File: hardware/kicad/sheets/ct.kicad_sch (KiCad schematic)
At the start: 30 parts, among them J12 CT, J13 AC_SENSE_DNP, U7 ADE7953ACPZ, Y1 3.579545MHz XO

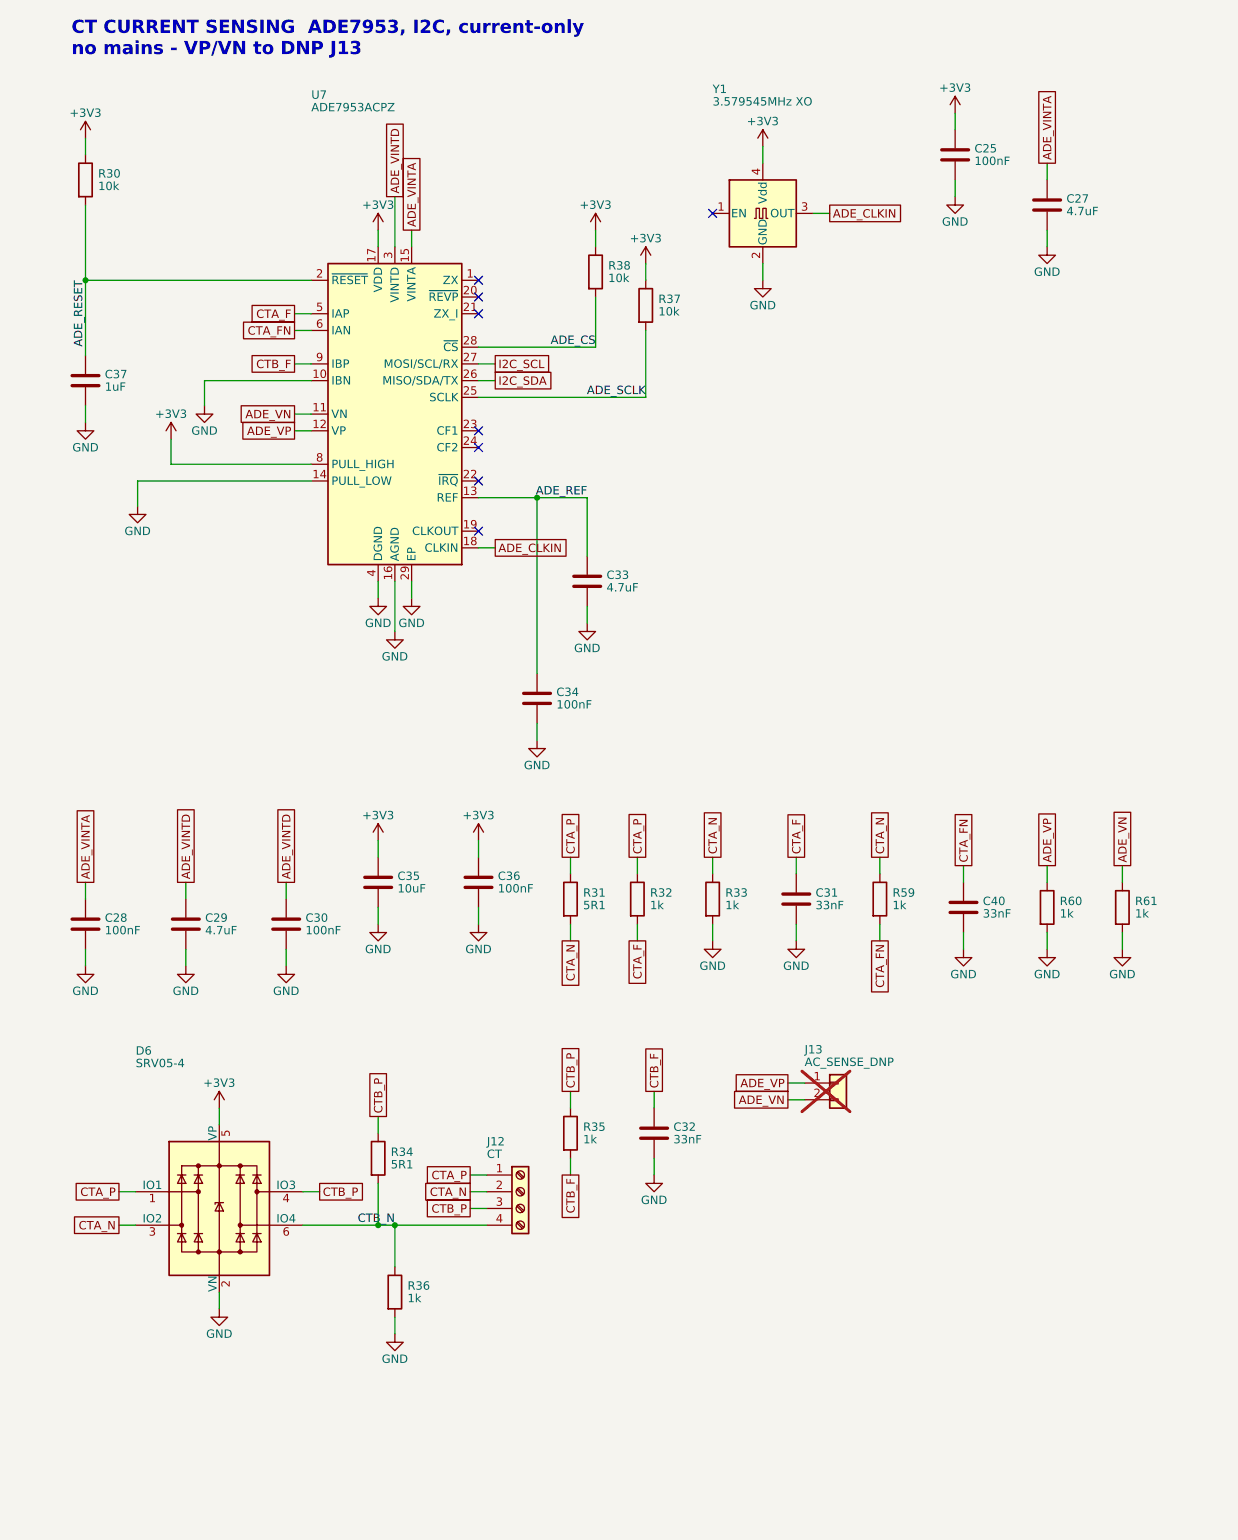
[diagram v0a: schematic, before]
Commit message: hardware: hierarchical schematic, ERC at 0/0, rev B.3
Applies items 1-3 of SCHEMATIC-REVIEW-2026-10-22.md.

ERC: the 173 lib_symbol_mismatch warnings were over-escaped quotes in the
embedded power symbols' Description strings; refreshed from the library.
The 18 off-grid power symbols are snapped and their stub wires redrawn.
The VIN and VLED global labels that existed only to carry a PWR_FLAG are
gone; the flags now sit on the nets they drive (J2.1, the VLED junction).
ERC reads 0 errors / 0 warnings with the documented SDO exclusion.

Hierarchy: no global labels remain. Each net that crosses sheets has one
hierarchical label per sheet, matching sheet pins on the root, and the
root wires those pins as a block diagram. Every other former global label
is a local label. The eight signal test points (TP4-TP11) move from the
test sheet to the mcu and ct sheets beside their nets, so the test block
needs no pins. KiCad names the nets /mcu/SPI_MISO etc.; netlist.py strips
the path, so the board's net names and the routing tables are unchanged
(182 components, 538 pads, 0 mismatches). single_global_label is now a
warning. check_sync_idempotent's collision fixture used the bare
"SPI_MISO" name and is updated, with a loud failure if its victims vanish.

Drawing: rev B.3 dated 2026-10-22 on every sheet, ct on A3 like the rest,
the three overflowing titles shortened, and the notes no longer refer to
design.py or to crystal load caps that no longer exist.

Co-Authored-By: Claude Fable 5.1 <noreply@anthropic.com>
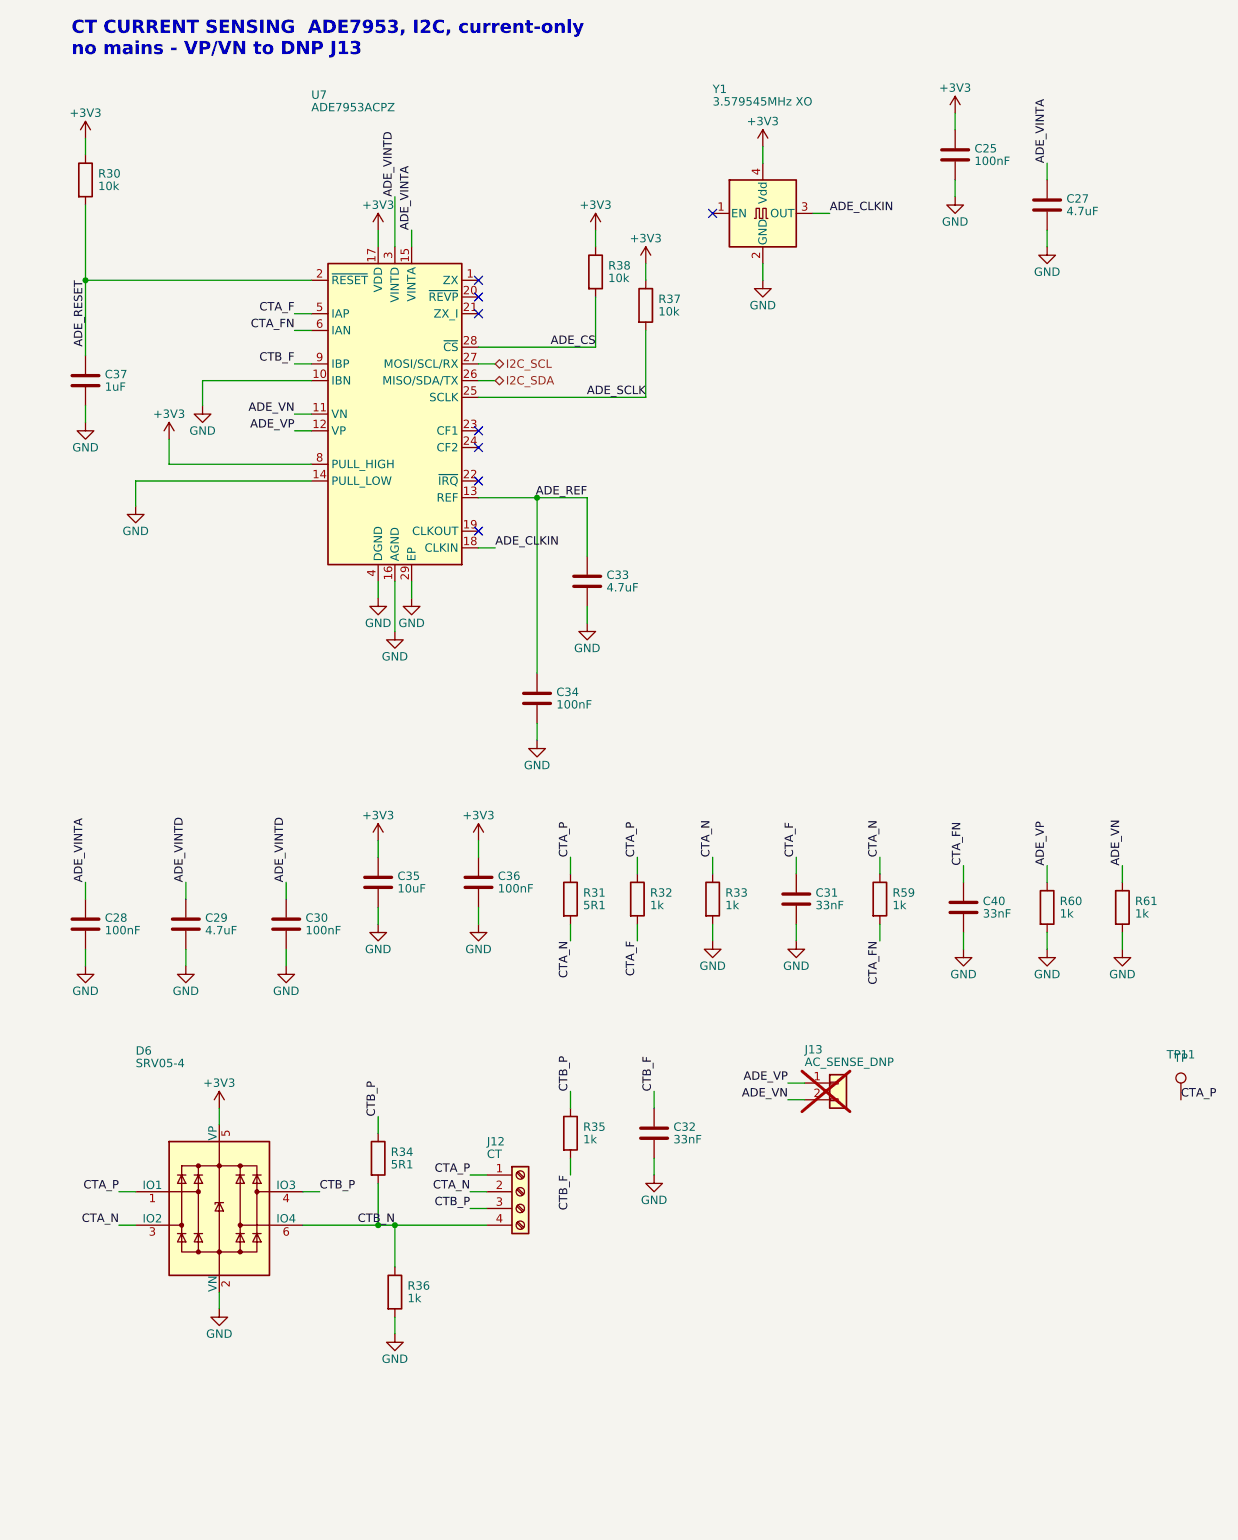
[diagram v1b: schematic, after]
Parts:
- added TP11: TP, TestPoint:TestPoint_Pad_D1.0mm, symbol Connector:TestPoint
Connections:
- net CTA_P: now also TP11.1

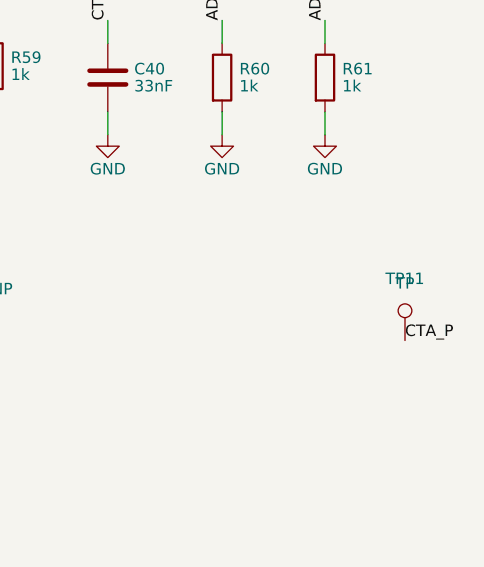
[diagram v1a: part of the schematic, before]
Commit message: hardware: flags at their sources, tri-state MAX31856, Q4 flipped, make erc
Second batch from SCHEMATIC-REVIEW-2026-10-22.md (findings 5, 7, 14, 15,
16 and the local half of 19).

PWR_FLAGs: the power sheet's parked corner is gone. Each flag now sits
where its rail is created - J2.1 (VIN), J2.2 (GND), Q8 source (VIN_P),
L1 output (BUCK_5V) and J1 pin A4 (VBUS, on the mcu sheet) - with the
value text shown on all of them.

MAX31856: U3 and U5 now use bisque:MAX31856 from the new project library
bisque.kicad_sym (registered in sym-lib-table), a copy of the KiCad
symbol with SDO typed tri-state, which is what the part does while CS is
high. The ERC exclusion that papered over the shared SPI_MISO is removed;
ERC is clean with no exclusions.

Q4 is mirrored so the high-side P-FET reads source-up to +5V and drain
down to SSR_EN. One Value string per LCSC part (C38/C44/C45 22uF/25V,
R11 100R 1%); C46 moved 5 mm right to clear the longer text. Every test
point's Value is its net name (TP1 "+3V3" ... TP12 "WDT_CT_P"), so the
board's Value fields, the JLC BOM and the schematic PDF regenerate.

make erc runs kicad-cli ERC at every severity and fails on any
violation; lib_symbol_mismatch, endpoint_off_grid and
same_local_global_label are promoted to errors in the project. It is not
part of pcb-check or CI on purpose.

Board: sync changed only Value fields (0 re-netted); gerbers differ by
timestamp only; DRC 0; full make pcb-check passes.

Co-Authored-By: Claude Fable 5.1 <noreply@anthropic.com>
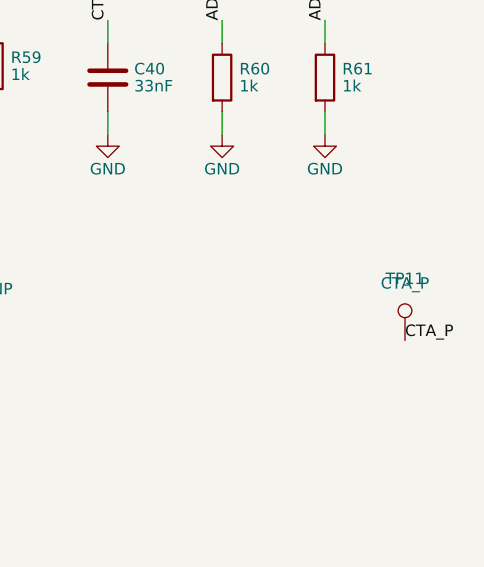
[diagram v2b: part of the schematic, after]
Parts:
- TP11: value TP -> CTA_P
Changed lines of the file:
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@@
 			)
 		)
-		(property "Value" "TP"
+		(property "Value" "CTA_P"
 			(at 190.5 184.15 0)
 			(show_name no)

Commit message: hardware: honest symbols, real MPNs, U6 spares grounded, LCD_RST verified
Third batch from SCHEMATIC-REVIEW-2026-10-22.md (findings 6, 8, 11, 17,
18 and E1/E2).

Symbols: D8 is bisque:SMAJ30A (drawn as a zener with its cathode on the
rail, since the fitted TVS is unidirectional), Q5-Q7 are bisque:CJ2310
and U2 is bisque:TLV1117LV33, each a flattened copy of the stock symbol
with the fitted part's name, description and LCSC-hosted datasheet, so
no pin or wire moved. The stock D_TVS, 2N7002 and TLV1117-33 embeds are
gone from the sheets.

Sourcing: every one of the 160 assembled symbols now carries MPN (the
manufacturer's part number, from LCSC's product record for its C-number),
Manufacturer and Datasheet (LCSC's hosted PDF) beside LCSC. check_mpn.py
keeps LCSC tied to gen_jlc.LCSC and requires the other two to be present
and MPN not to be a bare C-number.

Drawing: J11's IN1_RAW/IN2_RAW labels read along their own wires instead
of across the connector; U6's unused Darlington inputs I4-I7 are tied to
GND (the board's F.Cu pour already covers them - 4 pads re-netted, 0
unconnected, DRC 0); the root notes record the retired designators and
the LCD_RST finding (the MSP4021's own schematic shows no pull-up on
RESET, so GPIO46 does not block download mode); the mcu sheet notes that
GPIO35/36 rule out R8 (octal PSRAM) modules.

The datasheet manifest maps the shared 22uF/25V sheet to the unified
value and exempts the test points' net-name values. Full make pcb-check
passes; gerbers differ by timestamp and the re-filled GND pour; 3D
renders refreshed.

Co-Authored-By: Claude Fable 5.1 <noreply@anthropic.com>
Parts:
- C25, C28, C30, C34, C36: MPN C49678 -> CC0805KRX7R9BB104; Manufacturer (none) -> YAGEO
- C27, C29, C33: MPN C1779 -> CL21A475KAQNNNE; Manufacturer (none) -> Samsung Electro-Mechanics
- C31, C32, C40: MPN C1739 -> 0805B333K500NT; Manufacturer (none) -> FH
- C35: MPN C15850 -> CL21A106KAYNNNE; Manufacturer (none) -> Samsung Electro-Mechanics
- C37: MPN C28323 -> CL21B105KBFNNNE; Manufacturer (none) -> Samsung Electro-Mechanics
- D6: MPN C7420376 -> SRV05-4; Manufacturer (none) -> R+O
- J12: MPN C42377749 -> WJ500V-5.08-04P-14-00A; Manufacturer (none) -> KANGNEX
- R30, R37, R38: MPN C17414 -> 0805W8F1002T5E; Manufacturer (none) -> UNI-ROYAL
- R31, R34: MPN C17724 -> 0805W8F510KT5E; Manufacturer (none) -> UNI-ROYAL
- R32, R33, R35, R36, R59, R60, R61: MPN C17513 -> 0805W8F1001T5E; Manufacturer (none) -> UNI-ROYAL
- U7: MPN C515890 -> ADE7953ACPZ-RL; Manufacturer (none) -> ADI
- Y1: MPN C2838127 -> TFOM3.579545M4RHKCNT2T; Manufacturer (none) -> Yajingxin
